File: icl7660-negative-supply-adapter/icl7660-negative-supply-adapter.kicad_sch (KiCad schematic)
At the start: 11 parts, among them J1 Power Supply, J2 Eurorack_Power_Large, U1 ICL7660

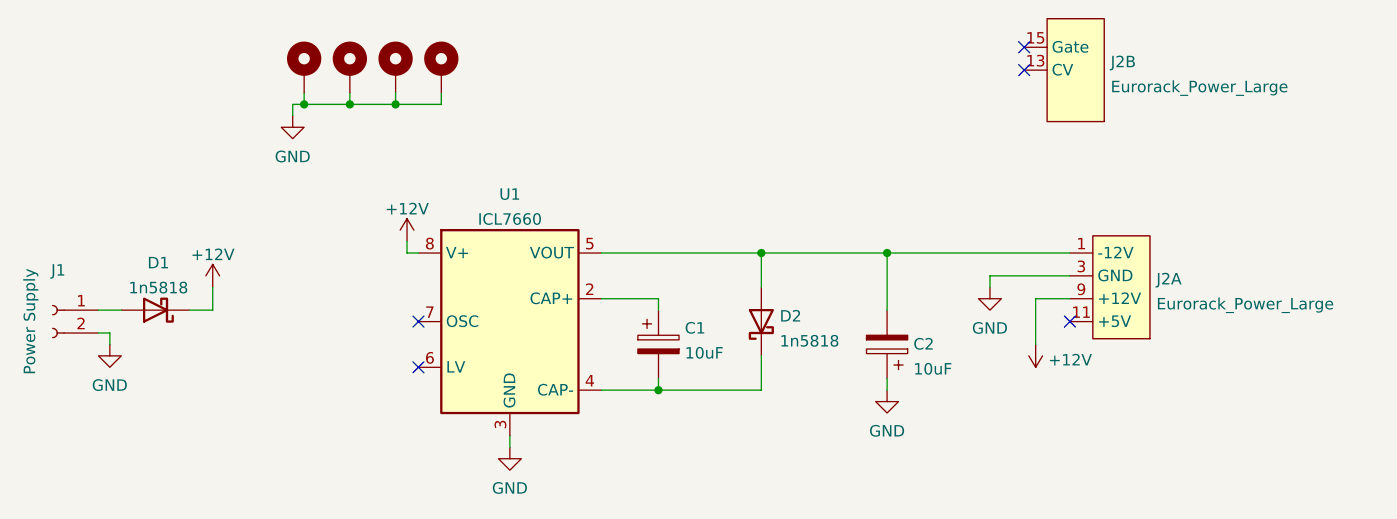
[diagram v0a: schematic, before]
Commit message: update iclc7660 adapter with new footprints
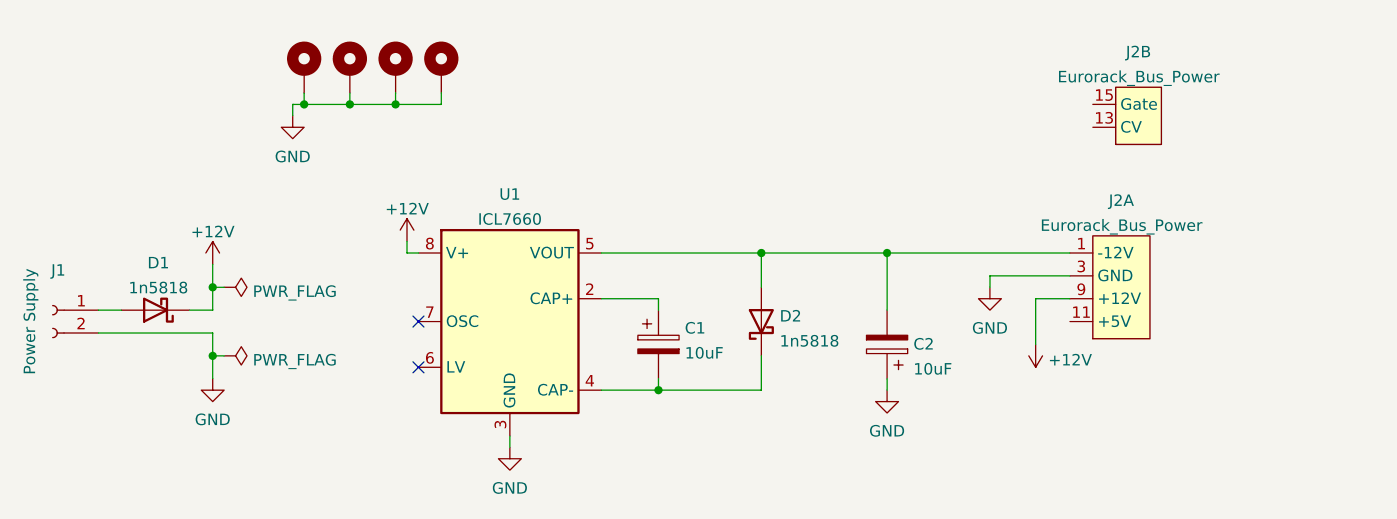
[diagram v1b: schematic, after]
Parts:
- removed J2: Eurorack_Power_Large, EurorackBasics:Eurorack_PowerHeader_2x08_P2.54mm_Shrouded, symbol Eurorack_Hardware:Eurorack_Power_Large
- added J2: Eurorack_Bus_Power, eurorack-power:Eurorack_PowerHeader_2x08_P2.54mm_Shrouded, symbol Eurorack_Hardware:Eurorack_Bus_Power
- C1, C2: footprint Rumblesan_Footprints:CP_Radial_D6.3mm_P2.50mm -> rumblesan-standard-parts:CP_Radial_D6.3mm_P2.50mm
- D1, D2: footprint Rumblesan_Footprints:D_DO-41_SOD81_P10.16mm_Horizontal -> rumblesan-standard-parts:D_DO-41_SOD81_P10.16mm_Horizontal
- H1, H2, H3, H4: footprint MountingHole:MountingHole_3.2mm_M3_DIN965_Pad -> rumblesan-standard-parts:MountingHole_3.2mm_M3_DIN965_Pad
- U1: footprint Rumblesan_Footprints:DIP-8_W7.62mm_Socket -> rumblesan-standard-parts:DIP-8_W7.62mm_Socket
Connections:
- net +12V: now also J2.10 (+12V), J2.9 (+12V)
- net GND: now also J2.3 (GND), J2.4 (GND), J2.5 (GND), J2.6 (GND), J2.7 (GND), J2.8 (GND)
- net at C2.2, D2.2 (A), U1.5 (VOUT): now also J2.1 (-12V), J2.2 (-12V)
- new net: J2.13 (CV), J2.14 (CV)
- new net: J2.15 (Gate), J2.16 (Gate)
- new net: J2.11 (+5V), J2.12 (+5V)
- no-connect marks 5 -> 2

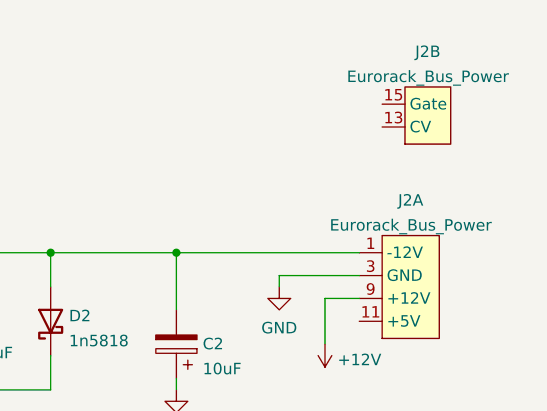
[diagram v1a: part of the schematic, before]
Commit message: Creating gerbers for negative supply adapter
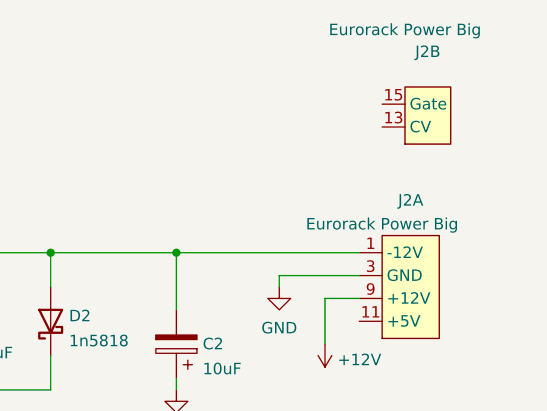
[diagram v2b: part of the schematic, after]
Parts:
- C1, C2: footprint rumblesan-standard-parts:CP_Radial_D6.3mm_P2.50mm -> rumblesan-standard-parts:CP_Radial_D5.0mm_P2.00mm; symbol Device:C_Polarized -> rumblesan-standard-parts:C_Polarized; Spec (none) -> electrolytic; Tolerance (none) -> 20%; Voltage (none) -> 50v
- H1, H2, H3, H4, J1: now left out of the parts list
- J2: value Eurorack_Bus_Power -> Eurorack Power Big; symbol Eurorack_Hardware:Eurorack_Bus_Power -> Eurorack_Hardware:Eurorack Bus Power
